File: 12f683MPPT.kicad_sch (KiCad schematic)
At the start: 51 parts, among them J1 Conn_01x01_Male, J2 Conn_01x01_Male, J3 Conn_01x01_Male, J4 Conn_01x01_Male, J5 Vin, J6 GND, J7 12V, Q1 BUK9511-55A127, Q2 BUK9511-55A127, Q3 2N2222A, Q4 2N2222A, Q5 2N2907A, SW1 SW_Push, U1 LM7805_TO220, U2 PIC12F683-IP, U3 LM358

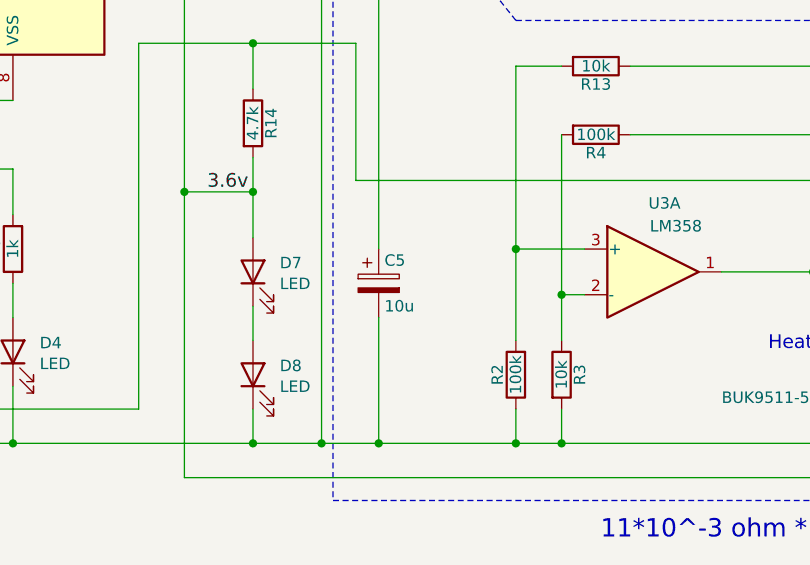
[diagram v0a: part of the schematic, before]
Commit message: Using ceramic capacitor.
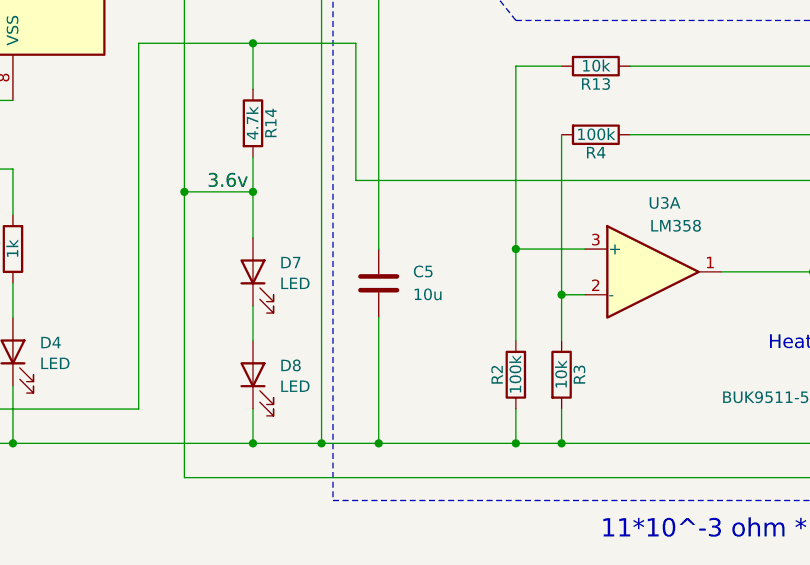
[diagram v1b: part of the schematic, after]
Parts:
- removed C5: 10u, Capacitor_THT:CP_Radial_D8.0mm_P2.50mm, symbol Device:CP
- added C5: 10u, symbol Device:C
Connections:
- net GNDPWR: now also C5.2
- net PV-Current: now also C5.1

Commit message: Change bootstrap diode D3 to 1N4148.
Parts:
- removed D3: 1N5819, Diode_THT:D_DO-41_SOD81_P10.16mm_Horizontal, symbol Device:D_Schottky
- added D3: 1N4148, Diode_THT:D_DO-41_SOD81_P10.16mm_Horizontal, symbol Device:D
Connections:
- net BootStrap: now also D3.1 (K)
- net at C3.1, C4.1, R11.1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: now also D3.2 (A)
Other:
- note removed: "D3 alternative = 1N4148"
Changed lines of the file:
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@@
 		)
 	)
-	(text "D3 alternative = 1N4148"
-		(exclude_from_sim no)
-		(at 138.684 53.594 0)
-		(effects
-			(font
-				(size 1.27 1.27)
-			)
-		)
-	)
 	(text "Optional"
 		(exclude_from_sim no)
@@
 	)
 	(symbol
-		(lib_id "Device:D_Schottky")
-		(at 138.43 59.69 180)
+		(lib_id "Connector:Conn_01x01_Pin")
+		(at 66.04 63.5 270)
 		(unit 1)
 		(body_style 1)
@@
 		(in_pos_files yes)
 		(dnp no)
-		(property "Reference" "D3"
-			(at 134.62 58.42 0)
+		(fields_autoplaced yes)
+		(property "Reference" "J6"
+			(at 67.31 62.8649 90)
 			(show_name no)
 			(do_not_autoplace no)
@@
 					(size 1.27 1.27)
 				)
+				(justify left)
 			)
 		)
-		(property "Value" "1N5819"
-			(at 138.43 63.5 0)
+		(property "Value" "GND"
+			(at 67.31 65.4049 90)
 			(show_name no)
 			(do_not_autoplace no)
@@
 					(size 1.27 1.27)
 				)
+				(justify left)
 			)
 		)
-		(property "Footprint" "Diode_THT:D_DO-41_SOD81_P10.16mm_Horizontal"
-			(at 138.43 59.69 0)
+		(property "Footprint" "Connector_Pin:Pin_D1.0mm_L10.0mm"
+			(at 66.04 63.5 0)
 			(hide yes)
 			(show_name no)
@@
 		)
 		(property "Datasheet" ""
-			(at 138.43 59.69 0)
+			(at 66.04 63.5 0)
 			(hide yes)
 			(show_name no)
@@
 			)
 		)
-		(property "Description" ""
-			(at 138.43 59.69 0)
+		(property "Description" "Generic connector, single row, 01x01, script generated"
+			(at 66.04 63.5 0)
+			(hide yes)
 			(show_name no)
 			(do_not_autoplace no)
@@
 			)
 		)
-		(pin "2"
-		)
 		(pin "1"
 		)
@@
 			(project "12f683MPPT"
 				(path "/c54864ce-ba59-4422-a8c7-824cf583dfc9"
-					(reference "D3")
+					(reference "J6")
 					(unit 1)
 				)
@@
 	)
 	(symbol
-		(lib_id "Connector:Conn_01x01_Pin")
-		(at 66.04 63.5 270)
+		(lib_id "Device:D_Zener")
+		(at 50.8 124.46 270)
 		(unit 1)
 		(body_style 1)
@@
 		(dnp no)
 		(fields_autoplaced yes)
-		(property "Reference" "J6"
-			(at 67.31 62.8649 90)
+		(property "Reference" "D10"
+			(at 53.34 123.1899 90)
 			(show_name no)
 			(do_not_autoplace no)
@@
 			)
 		)
-		(property "Value" "GND"
-			(at 67.31 65.4049 90)
+		(property "Value" "1N5227B"
+			(at 53.34 125.7299 90)
 			(show_name no)
 			(do_not_autoplace no)
@@
 			)
 		)
-		(property "Footprint" "Connector_Pin:Pin_D1.0mm_L10.0mm"
-			(at 66.04 63.5 0)
+		(property "Footprint" "Diode_THT:D_DO-41_SOD81_P7.62mm_Horizontal"
+			(at 50.8 124.46 0)
 			(hide yes)
 			(show_name no)
@@
 		)
 		(property "Datasheet" ""
-			(at 66.04 63.5 0)
+			(at 50.8 124.46 0)
 			(hide yes)
 			(show_name no)
@@
 			)
 		)
-		(property "Description" "Generic connector, single row, 01x01, script generated"
-			(at 66.04 63.5 0)
+		(property "Description" "Zener diode"
+			(at 50.8 124.46 0)
 			(hide yes)
 			(show_name no)
@@
 			)
 		)
+		(pin "2"
+		)
 		(pin "1"
 		)
@@
 			(project "12f683MPPT"
 				(path "/c54864ce-ba59-4422-a8c7-824cf583dfc9"
-					(reference "J6")
+					(reference "D10")
 					(unit 1)
 				)
@@
 	)
 	(symbol
-		(lib_id "Device:D_Zener")
-		(at 50.8 124.46 270)
+		(lib_id "Device:C")
+		(at 154.94 124.46 0)
 		(unit 1)
 		(body_style 1)
@@
 		(dnp no)
 		(fields_autoplaced yes)
-		(property "Reference" "D10"
-			(at 53.34 123.1899 90)
+		(property "Reference" "C5"
+			(at 158.75 123.1899 0)
 			(show_name no)
 			(do_not_autoplace no)
@@
 			)
 		)
-		(property "Value" "1N5227B"
-			(at 53.34 125.7299 90)
+		(property "Value" "10u"
+			(at 158.75 125.7299 0)
 			(show_name no)
 			(do_not_autoplace no)
@@
 			)
 		)
-		(property "Footprint" "Diode_THT:D_DO-41_SOD81_P7.62mm_Horizontal"
-			(at 50.8 124.46 0)
+		(property "Footprint" ""
+			(at 155.9052 128.27 0)
 			(hide yes)
 			(show_name no)
@@
 		)
 		(property "Datasheet" ""
-			(at 50.8 124.46 0)
+			(at 154.94 124.46 0)
 			(hide yes)
 			(show_name no)
@@
 			)
 		)
-		(property "Description" "Zener diode"
-			(at 50.8 124.46 0)
+		(property "Description" "Unpolarized capacitor"
+			(at 154.94 124.46 0)
 			(hide yes)
 			(show_name no)
@@
 			)
 		)
-		(pin "2"
-		)
 		(pin "1"
 		)
+		(pin "2"
+		)
 		(instances
 			(project "12f683MPPT"
 				(path "/c54864ce-ba59-4422-a8c7-824cf583dfc9"
-					(reference "D10")
+					(reference "C5")
 					(unit 1)
 				)
@@
 	)
 	(symbol
-		(lib_id "Device:C")
-		(at 154.94 124.46 0)
+		(lib_id "Connector:Conn_01x01_Pin")
+		(at 73.66 63.5 270)
 		(unit 1)
 		(body_style 1)
@@
 		(dnp no)
 		(fields_autoplaced yes)
-		(property "Reference" "C5"
-			(at 158.75 123.1899 0)
+		(property "Reference" "J7"
+			(at 74.93 62.8649 90)
 			(show_name no)
 			(do_not_autoplace no)
@@
 			)
 		)
-		(property "Value" "10u"
-			(at 158.75 125.7299 0)
+		(property "Value" "12V"
+			(at 74.93 65.4049 90)
 			(show_name no)
 			(do_not_autoplace no)
@@
 			)
 		)
-		(property "Footprint" ""
-			(at 155.9052 128.27 0)
+		(property "Footprint" "Connector_Pin:Pin_D1.0mm_L10.0mm"
+			(at 73.66 63.5 0)
 			(hide yes)
 			(show_name no)
@@
 		)
 		(property "Datasheet" ""
-			(at 154.94 124.46 0)
+			(at 73.66 63.5 0)
 			(hide yes)
 			(show_name no)
@@
 			)
 		)
-		(property "Description" "Unpolarized capacitor"
-			(at 154.94 124.46 0)
+		(property "Description" "Generic connector, single row, 01x01, script generated"
+			(at 73.66 63.5 0)
 			(hide yes)
 			(show_name no)
@@
 		(pin "1"
 		)
-		(pin "2"
-		)
 		(instances
 			(project "12f683MPPT"
 				(path "/c54864ce-ba59-4422-a8c7-824cf583dfc9"
-					(reference "C5")
+					(reference "J7")
 					(unit 1)
 				)
@@
 	)
 	(symbol
-		(lib_id "Connector:Conn_01x01_Pin")
-		(at 73.66 63.5 270)
+		(lib_id "Device:D")
+		(at 138.43 59.69 180)
 		(unit 1)
 		(body_style 1)
@@
 		(in_pos_files yes)
 		(dnp no)
-		(fields_autoplaced yes)
-		(property "Reference" "J7"
-			(at 74.93 62.8649 90)
+		(property "Reference" "D3"
+			(at 135.128 62.992 0)
 			(show_name no)
 			(do_not_autoplace no)
@@
 					(size 1.27 1.27)
 				)
-				(justify left)
 			)
 		)
-		(property "Value" "12V"
-			(at 74.93 65.4049 90)
+		(property "Value" "1N4148"
+			(at 141.478 62.992 0)
 			(show_name no)
 			(do_not_autoplace no)
@@
 					(size 1.27 1.27)
 				)
-				(justify left)
 			)
 		)
-		(property "Footprint" "Connector_Pin:Pin_D1.0mm_L10.0mm"
-			(at 73.66 63.5 0)
+		(property "Footprint" "Diode_THT:D_DO-41_SOD81_P10.16mm_Horizontal"
+			(at 138.43 59.69 0)
 			(hide yes)
 			(show_name no)
@@
 		)
 		(property "Datasheet" ""
-			(at 73.66 63.5 0)
+			(at 138.43 59.69 0)
 			(hide yes)
 			(show_name no)
@@
 			)
 		)
-		(property "Description" "Generic connector, single row, 01x01, script generated"
-			(at 73.66 63.5 0)
+		(property "Description" "Diode"
+			(at 138.43 59.69 0)
 			(hide yes)
 			(show_name no)
@@
 			)
 		)
+		(property "Sim.Device" "D"
+			(at 138.43 59.69 0)
+			(hide yes)
+			(show_name no)
+			(do_not_autoplace no)
+			(effects
+				(font
+					(size 1.27 1.27)
+				)
+			)
+		)
+		(property "Sim.Pins" "1=K 2=A"
+			(at 138.43 59.69 0)
+			(hide yes)
+			(show_name no)
+			(do_not_autoplace no)
+			(effects
+				(font
+					(size 1.27 1.27)
+				)
+			)
+		)
+		(pin "2"
+		)
 		(pin "1"
 		)
@@
 			(project "12f683MPPT"
 				(path "/c54864ce-ba59-4422-a8c7-824cf583dfc9"
-					(reference "J7")
+					(reference "D3")
 					(unit 1)
 				)

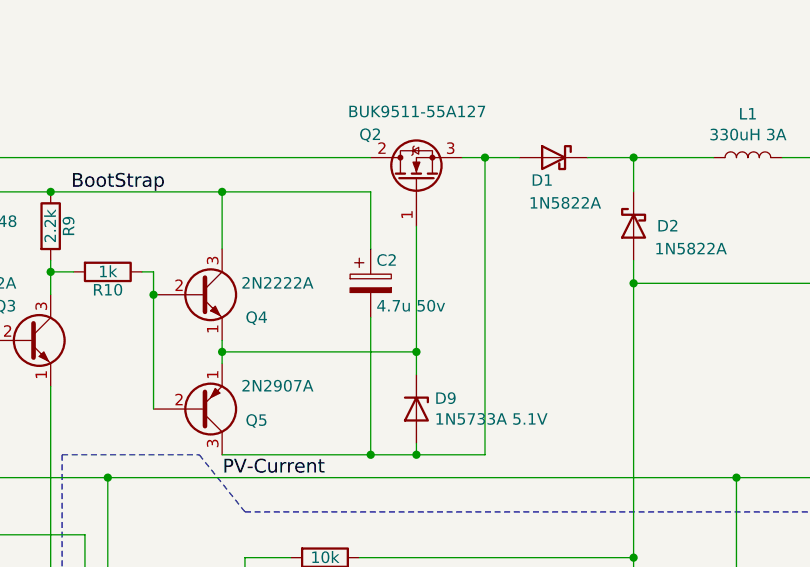
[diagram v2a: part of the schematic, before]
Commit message: Change C2 to 1uF ceramic.
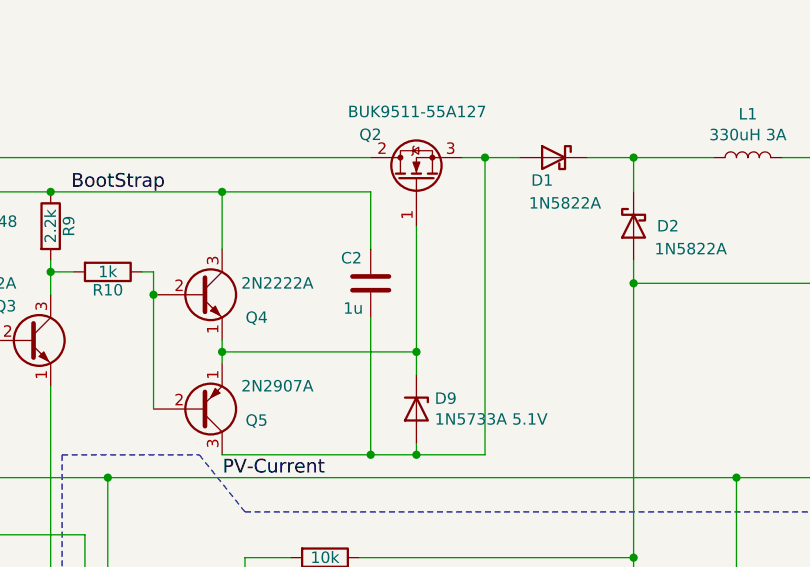
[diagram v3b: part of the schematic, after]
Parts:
- removed C2: 4.7u 50v, Capacitor_THT:CP_Radial_D8.0mm_P2.50mm, symbol Device:CP
- added C2: 1u, symbol Device:C
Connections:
- net BootStrap: now also C2.1
- net at D1.2 (A), D9.2 (A), Q2.3 (S)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: now also C2.2
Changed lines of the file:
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@@
 	)
 	(symbol
-		(lib_id "Device:CP")
-		(at 184.15 69.85 0)
-		(unit 1)
-		(body_style 1)
-		(exclude_from_sim no)
-		(in_bom yes)
-		(on_board yes)
-		(in_pos_files yes)
-		(dnp no)
-		(property "Reference" "C2"
-			(at 184.785 67.31 0)
-			(show_name no)
-			(do_not_autoplace no)
-			(effects
-				(font
-					(size 1.27 1.27)
-				)
-				(justify left)
-			)
-		)
-		(property "Value" "4.7u 50v"
-			(at 184.785 72.39 0)
-			(show_name no)
-			(do_not_autoplace no)
-			(effects
-				(font
-					(size 1.27 1.27)
-				)
-				(justify left)
-			)
-		)
-		(property "Footprint" "Capacitor_THT:CP_Radial_D8.0mm_P2.50mm"
-			(at 185.1152 73.66 0)
-			(hide yes)
-			(show_name no)
-			(do_not_autoplace no)
-			(effects
-				(font
-					(size 0.762 0.762)
-				)
-			)
-		)
-		(property "Datasheet" ""
-			(at 184.15 69.85 0)
-			(show_name no)
-			(do_not_autoplace no)
-			(effects
-				(font
-					(size 1.524 1.524)
-				)
-			)
-		)
-		(property "Description" ""
-			(at 184.15 69.85 0)
-			(show_name no)
-			(do_not_autoplace no)
-			(effects
-				(font
-					(size 1.27 1.27)
-				)
-			)
-		)
-		(pin "1"
-		)
-		(pin "2"
-		)
-		(instances
-			(project "12f683MPPT"
-				(path "/c54864ce-ba59-4422-a8c7-824cf583dfc9"
-					(reference "C2")
-					(unit 1)
-				)
-			)
-		)
-	)
-	(symbol
 		(lib_id "Device:Q_NPN_EBC")
 		(at 146.05 76.2 0)
@@
 					(unit 1)
 				)
+			)
+		)
+	)
+	(symbol
+		(lib_id "Device:C")
+		(at 184.15 69.85 0)
+		(unit 1)
+		(body_style 1)
+		(exclude_from_sim no)
+		(in_bom yes)
+		(on_board yes)
+		(in_pos_files yes)
+		(dnp no)
+		(property "Reference" "C2"
+			(at 180.848 67.056 0)
+			(show_name no)
+			(do_not_autoplace no)
+			(effects
+				(font
+					(size 1.27 1.27)
+				)
+				(justify left)
+			)
+		)
+		(property "Value" "1u"
+			(at 181.102 72.644 0)
+			(show_name no)
+			(do_not_autoplace no)
+			(effects
+				(font
+					(size 1.27 1.27)
+				)
+				(justify left)
+			)
+		)
+		(property "Footprint" ""
+			(at 185.1152 73.66 0)
+			(hide yes)
+			(show_name no)
+			(do_not_autoplace no)
+			(effects
+				(font
+					(size 1.27 1.27)
+				)
+			)
+		)
+		(property "Datasheet" ""
+			(at 184.15 69.85 0)
+			(hide yes)
+			(show_name no)
+			(do_not_autoplace no)
+			(effects
+				(font
+					(size 1.27 1.27)
+				)
+			)
+		)
+		(property "Description" "Unpolarized capacitor"
+			(at 184.15 69.85 0)
+			(hide yes)
+			(show_name no)
+			(do_not_autoplace no)
+			(effects
+				(font
+					(size 1.27 1.27)
+				)
+			)
+		)
+		(pin "1"
+		)
+		(pin "2"
+		)
+		(instances
+			(project "12f683MPPT"
+				(path "/c54864ce-ba59-4422-a8c7-824cf583dfc9"
+					(reference "C2")
+					(unit 1)
+				)

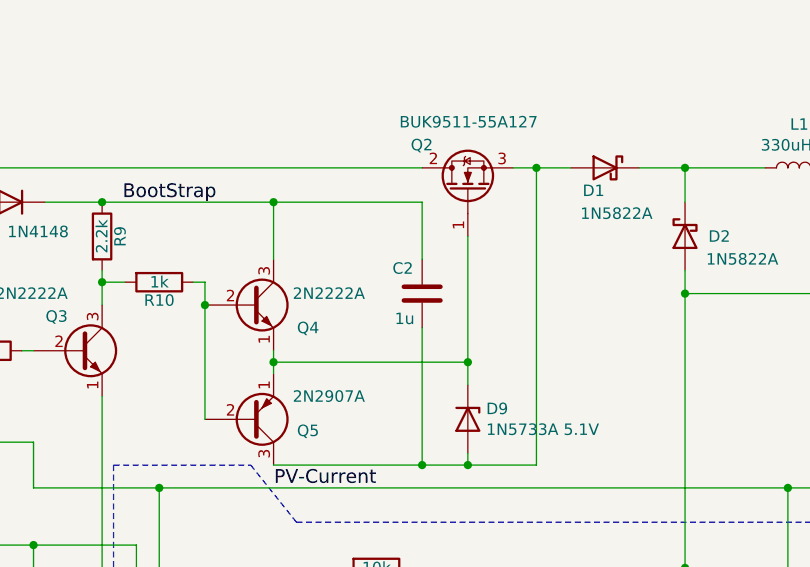
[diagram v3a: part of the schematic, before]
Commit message: Update foot print.
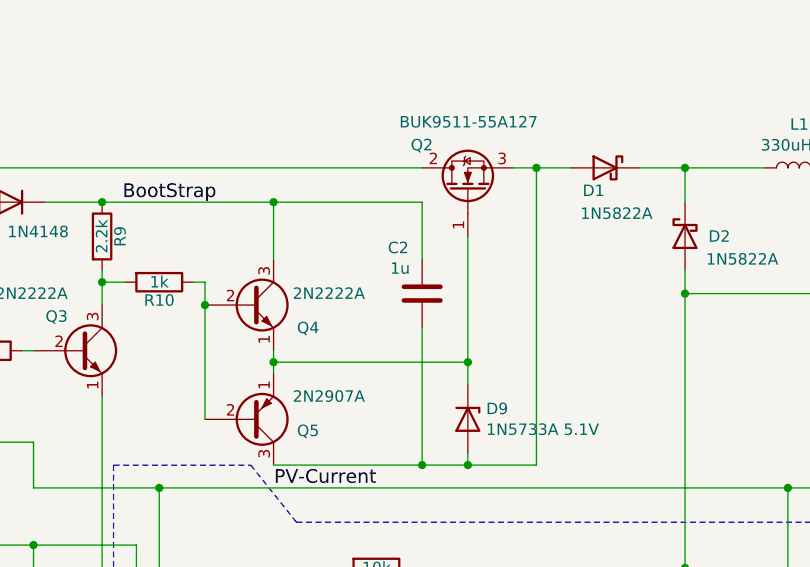
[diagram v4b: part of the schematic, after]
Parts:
- C2: footprint (none) -> Capacitor_THT:C_Disc_D7.5mm_W4.4mm_P5.00mm
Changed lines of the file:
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@@
 		(dnp no)
 		(property "Reference" "C2"
-			(at 180.848 67.056 0)
+			(at 180.34 64.77 0)
 			(show_name no)
 			(do_not_autoplace no)
@@
 		)
 		(property "Value" "1u"
-			(at 181.102 72.644 0)
+			(at 180.594 67.056 0)
 			(show_name no)
 			(do_not_autoplace no)
@@
 			)
 		)
-		(property "Footprint" ""
+		(property "Footprint" "Capacitor_THT:C_Disc_D7.5mm_W4.4mm_P5.00mm"
 			(at 185.1152 73.66 0)
 			(hide yes)
